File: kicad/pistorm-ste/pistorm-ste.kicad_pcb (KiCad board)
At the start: 4 copper layers, 105.5 x 44.2 mm, 31 parts, among them J1 Raspberry_Pi_2_3, J2 Conn_01x02_Male, U1 SN54CBTD3384, U2 SN74LVC16373, U3 SN74LVC16373, U4 EPM240T100, U5 SN74LVC16373, U6 SN74LVC16373, U7 SN54CBTD3384, U8 LM1117-3.3

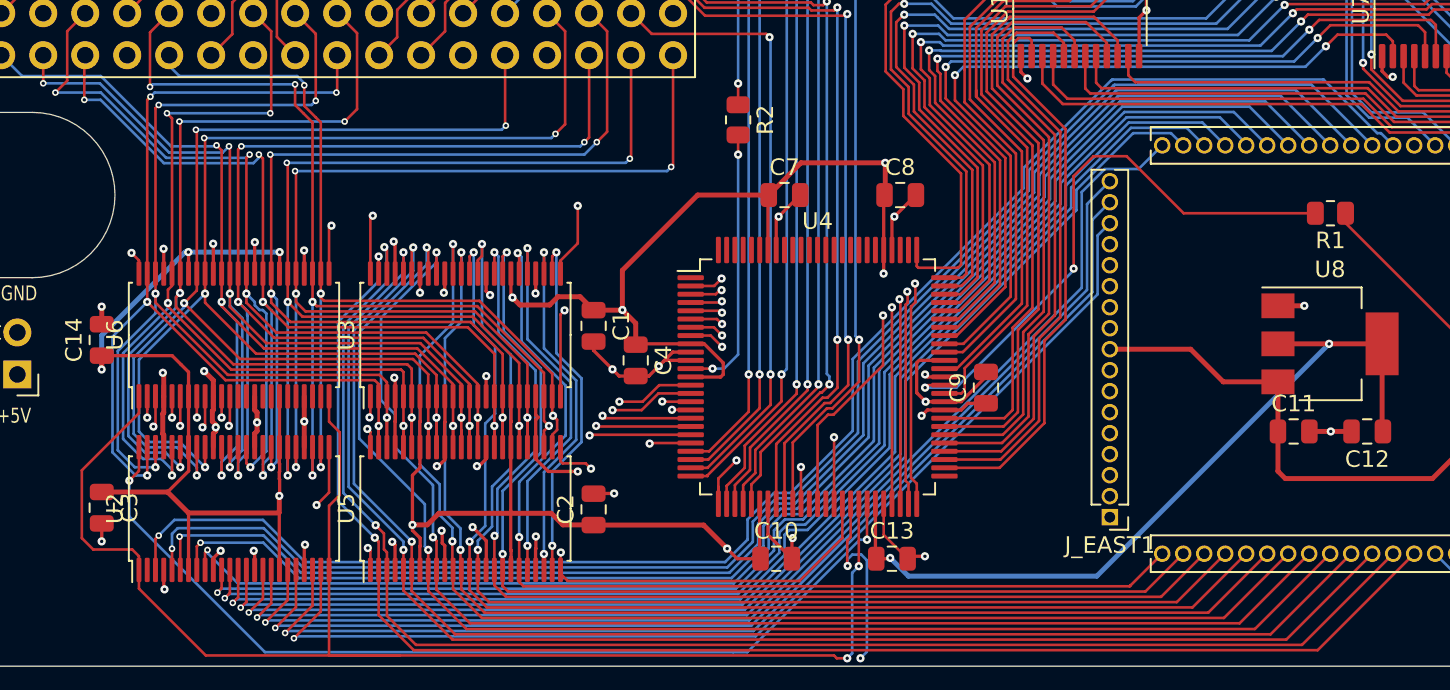
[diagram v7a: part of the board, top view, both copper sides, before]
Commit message: Routing complete and passing DRC. Query PLCC socket alignment. Will change to a single footprint.
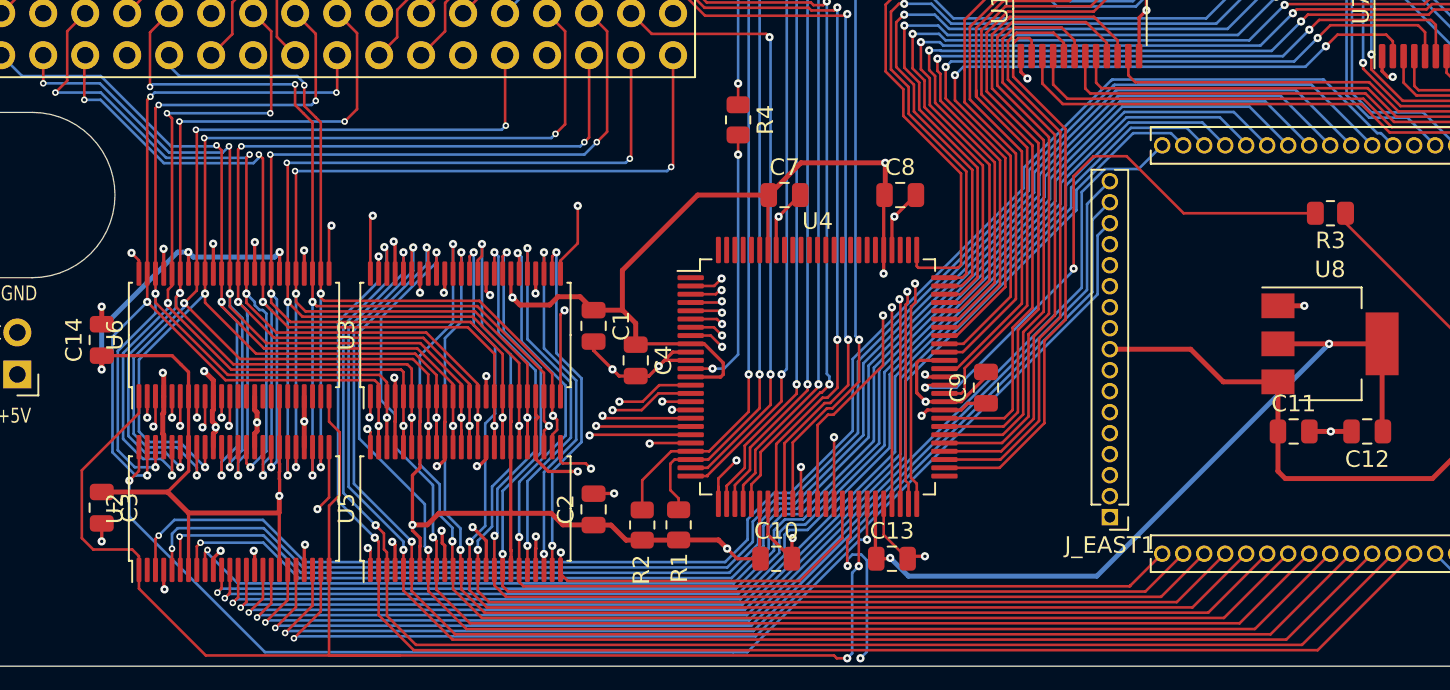
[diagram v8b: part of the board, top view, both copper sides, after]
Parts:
- added R1: 4k7, Resistor_SMD:R_0805_2012Metric, F.Cu at (109.7, 150.4)
- added R2: 4k7, Resistor_SMD:R_0805_2012Metric, F.Cu at (107.5, 150.4)
- renumbered R1 to R3, R2 to R4
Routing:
- net /TMS: track 66.8 -> 72.2 mm
- net /TDI: track 71.6 -> 75.9 mm
- net +3V3: track 296.9 -> 297.9 mm, vias 15 -> 14
